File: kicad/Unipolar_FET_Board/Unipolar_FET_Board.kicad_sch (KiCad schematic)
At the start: 18 parts, among them J1 Screw_Terminal_01x04, J3 SENSE, J4 N-MOS, Q1 Q_NMOS_GDS, Q2 Q_NMOS_GDS

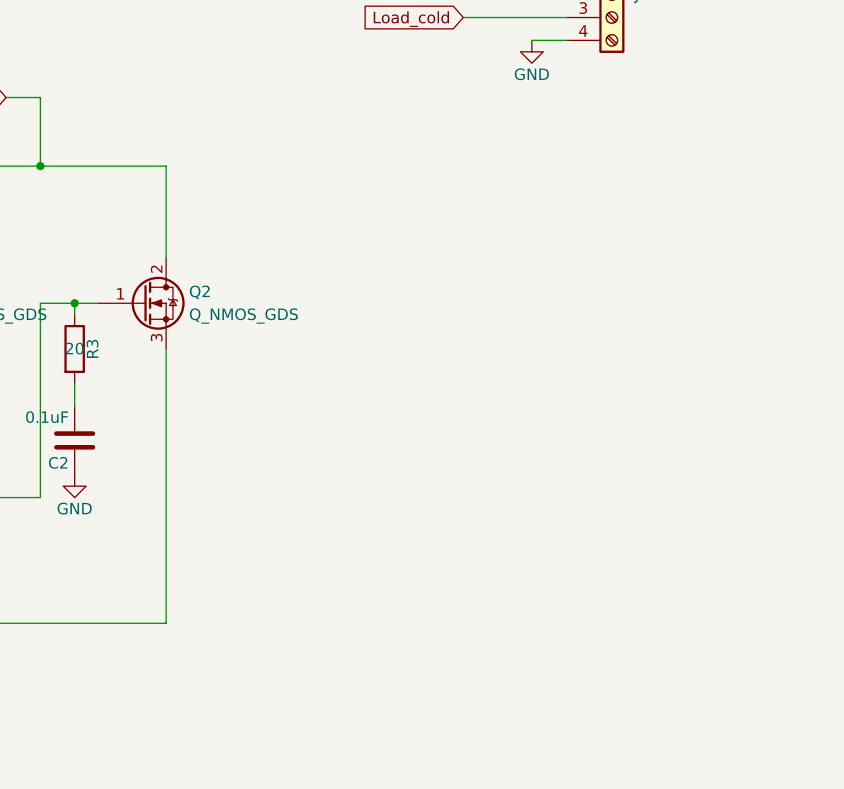
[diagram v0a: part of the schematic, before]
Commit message: Added varistor and labesl for the connecters
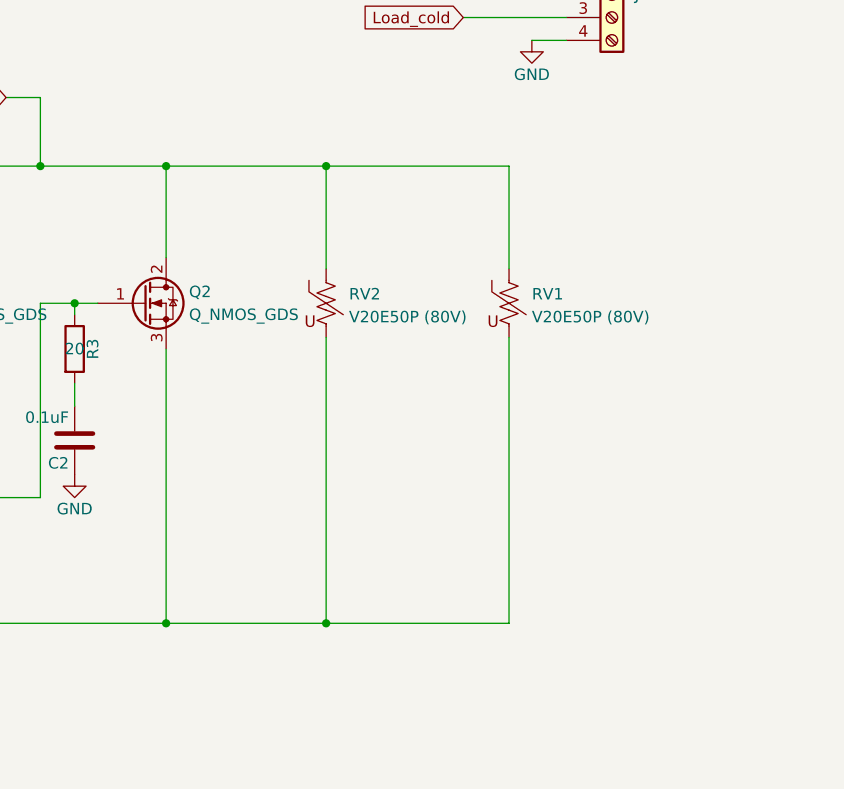
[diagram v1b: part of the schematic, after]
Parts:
- added RV1, RV2: V20E50P (80V), Varistor:RV_Disc_D15.5mm_W7.5mm_P7.5mm, symbol Device:Varistor_US
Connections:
- net Load_cold: now also RV1.1, RV2.1
- net at Q1.3 (S), Q2.3 (S), R9.1: now also RV1.2, RV2.2

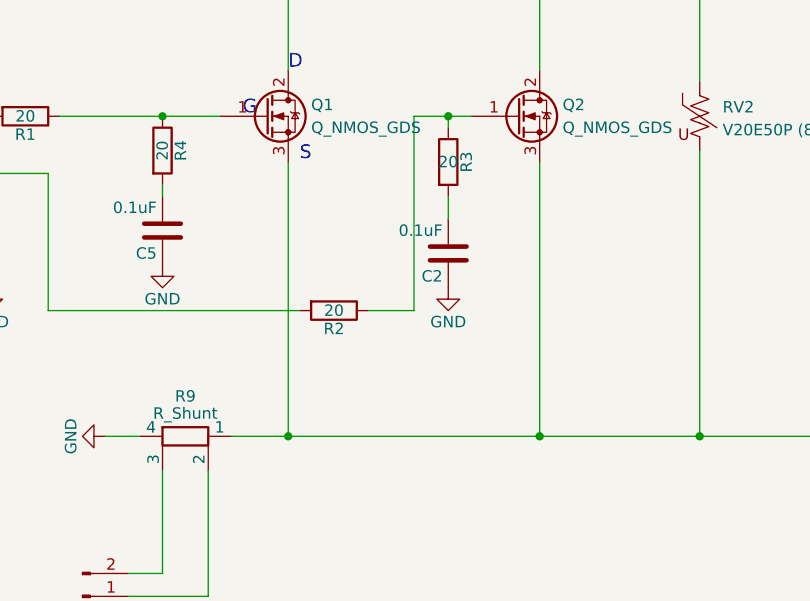
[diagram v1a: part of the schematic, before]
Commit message: Parallel MOS with current sharing resistors
Putting additional resistors in series with the source of each MOS is not necessary.
Nonetheless I saved this partiular snapshot in case we want to pursuit this strategy to share the current
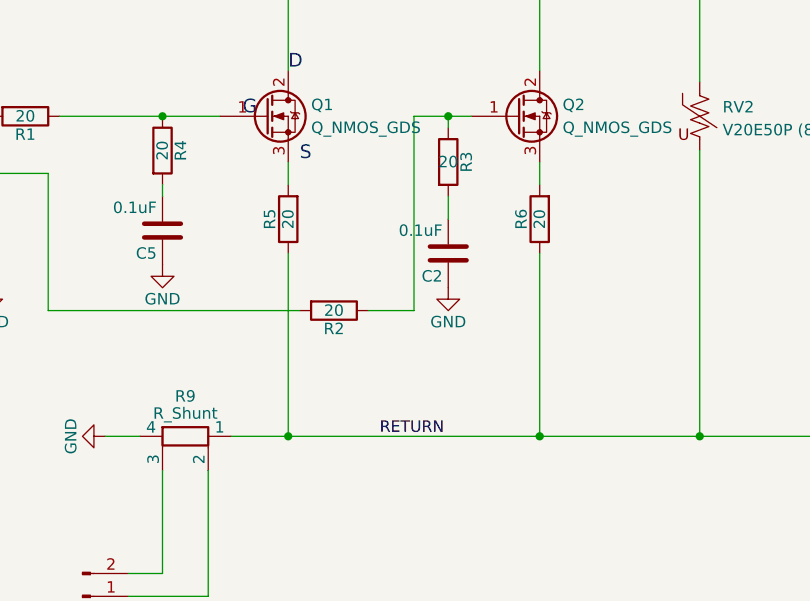
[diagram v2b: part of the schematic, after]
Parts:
- added R5, R6: 20, zmyfootprint:res_2818, symbol rear-rescue:R-rear-rescue
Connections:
- net RETURN: now reaches R9.1, RV1.2, RV2.2
- net RETURN: now also R5.1, R6.1; no longer Q1.3 (S), Q2.3 (S)
- new net: Q1.3 (S), R5.2
- new net: Q2.3 (S), R6.2
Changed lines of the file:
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@@
+	)
+	(junction
+		(at 134.62 104.14)
+		(diameter 0)
+		(color 0 0 0 0)
 	)
 	(junction
@@
 		(color 0 0 0 0)
 	)
-	(junction
-		(at 134.62 104.14)
-		(diameter 0)
-		(color 0 0 0 0)
-	)
 	(wire
 		(pts
@@
 	(wire
 		(pts
+			(xy 162.56 73.66) (xy 162.56 76.2)
+		)
+		(stroke
+			(width 0)
+			(type default)
+		)
+	)
+	(wire
+		(pts
 			(xy 66.04 35.56) (xy 66.04 39.37)
 		)
@@
 	(wire
 		(pts
-			(xy 162.56 73.66) (xy 162.56 104.14)
-		)
-		(stroke
-			(width 0)
-			(type default)
-		)
-	)
-	(wire
-		(pts
 			(xy 109.22 68.58) (xy 120.65 68.58)
 		)
@@
 	(wire
 		(pts
-			(xy 134.62 73.66) (xy 134.62 104.14)
+			(xy 134.62 73.66) (xy 134.62 76.2)
 		)
 		(stroke
@@
 	(wire
 		(pts
+			(xy 162.56 104.14) (xy 134.62 104.14)
+		)
+		(stroke
+			(width 0)
+			(type default)
+		)
+	)
+	(wire
+		(pts
 			(xy 152.4 68.58) (xy 154.94 68.58)
 		)
@@
 	(wire
 		(pts
+			(xy 162.56 83.82) (xy 162.56 104.14)
+		)
+		(stroke
+			(width 0)
+			(type default)
+		)
+	)
+	(wire
+		(pts
 			(xy 200.66 64.77) (xy 200.66 53.34)
 		)
@@
 	(wire
 		(pts
-			(xy 162.56 104.14) (xy 134.62 104.14)
-		)
-		(stroke
-			(width 0)
-			(type default)
-		)
-	)
-	(wire
-		(pts
 			(xy 200.66 31.75) (xy 200.66 33.02)
+		)
+		(stroke
+			(width 0)
+			(type default)
+		)
+	)
+	(wire
+		(pts
+			(xy 134.62 83.82) (xy 134.62 104.14)
 		)
 		(stroke
@@
 			(font
 				(size 1.524 1.524)
+			)
+			(justify left bottom)
+		)
+	)
+	(label "RETURN"
+		(at 144.78 104.14 0)
+		(fields_autoplaced yes)
+		(effects
+			(font
+				(size 1.27 1.27)
 			)
 			(justify left bottom)
@@
 	)
 	(symbol
+		(lib_id "rear-rescue:R-rear-rescue")
+		(at 134.62 80.01 180)
+		(unit 1)
+		(exclude_from_sim no)
+		(in_bom yes)
+		(on_board yes)
+		(dnp no)
+		(property "Reference" "R5"
+			(at 132.588 80.01 90)
+			(effects
+				(font
+					(size 1.27 1.27)
+				)
+			)
+		)
+		(property "Value" "20"
+			(at 134.62 80.01 90)
+			(effects
+				(font
+					(size 1.27 1.27)
+				)
+			)
+		)
+		(property "Footprint" "zmyfootprint:res_2818"
+			(at 136.398 80.01 90)
+			(effects
+				(font
+					(size 1.27 1.27)
+				)
+				(hide yes)
+			)
+		)
+		(property "Datasheet" ""
+			(at 134.62 80.01 0)
+			(effects
+				(font
+					(size 1.27 1.27)
+				)
+				(hide yes)
+			)
+		)
+		(property "Description" ""
+			(at 134.62 80.01 0)
+			(effects
+				(font
+					(size 1.27 1.27)
+				)
+				(hide yes)
+			)
+		)
+		(property "DIGIKEY" "541-3276-1-ND"
+			(at 134.62 80.01 90)
+			(effects
+				(font
+					(size 1.27 1.27)
+				)
+				(hide yes)
+			)
+		)
+		(property "PARTNO" "WSHP2818R0100FEA"
+			(at 134.62 80.01 90)
+			(effects
+				(font
+					(size 1.27 1.27)
+				)
+				(hide yes)
+			)
+		)
+		(pin "1"
+		)
+		(pin "2"
+		)
+		(instances
+			(project "Unipolar_FET_Board"
+				(path "/2f21daab-ac04-42a8-876c-c86138d20a60"
+					(reference "R5")
+					(unit 1)
+				)
+			)
+		)
+	)
+	(symbol
 		(lib_id "Connector:Conn_01x02_Pin")
 		(at 93.98 83.82 0)
@@
 					(unit 1)
 				)
+			)
+		)
+	)
+	(symbol
+		(lib_id "rear-rescue:R-rear-rescue")
+		(at 162.56 80.01 180)
+		(unit 1)
+		(exclude_from_sim no)
+		(in_bom yes)
+		(on_board yes)
+		(dnp no)
+		(property "Reference" "R6"
+			(at 160.528 80.01 90)
+			(effects
+				(font
+					(size 1.27 1.27)
+				)
+			)
+		)
+		(property "Value" "20"
+			(at 162.56 80.01 90)
+			(effects
+				(font
+					(size 1.27 1.27)
+				)
+			)
+		)
+		(property "Footprint" "zmyfootprint:res_2818"
+			(at 164.338 80.01 90)
+			(effects
+				(font
+					(size 1.27 1.27)
+				)
+				(hide yes)
+			)
+		)
+		(property "Datasheet" ""
+			(at 162.56 80.01 0)
+			(effects
+				(font
+					(size 1.27 1.27)
+				)
+				(hide yes)
+			)
+		)
+		(property "Description" ""
+			(at 162.56 80.01 0)
+			(effects
+				(font
+					(size 1.27 1.27)
+				)
+				(hide yes)
+			)
+		)
+		(property "DIGIKEY" "541-3276-1-ND"
+			(at 162.56 80.01 90)
+			(effects
+				(font
+					(size 1.27 1.27)
+				)
+				(hide yes)
+			)
+		)
+		(property "PARTNO" "WSHP2818R0100FEA"
+			(at 162.56 80.01 90)
+			(effects
+				(font
+					(size 1.27 1.27)
+				)
+				(hide yes)
+			)
+		)
+		(pin "1"
+		)
+		(pin "2"
+		)
+		(instances
+			(project "Unipolar_FET_Board"
+				(path "/2f21daab-ac04-42a8-876c-c86138d20a60"
+					(reference "R6")
+					(unit 1)
+				)

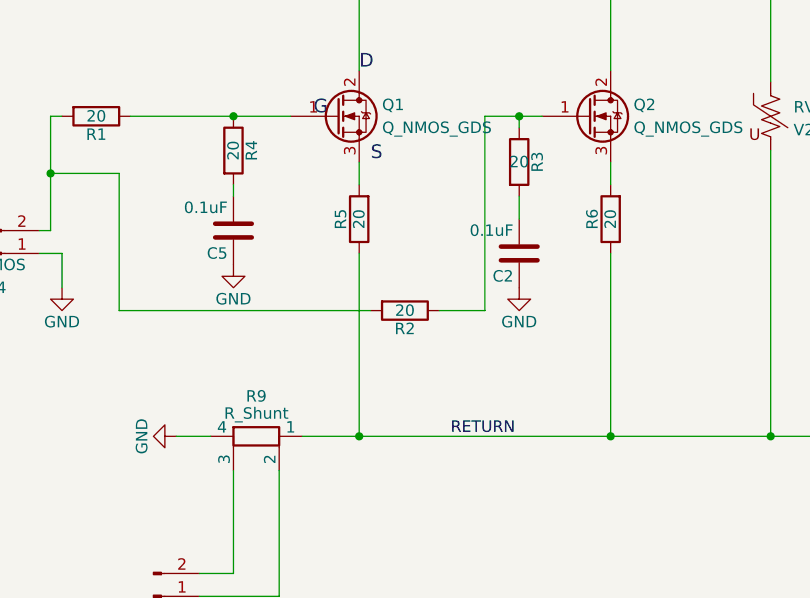
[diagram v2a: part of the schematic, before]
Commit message: The MOS and capacitors are now in the correct orientation
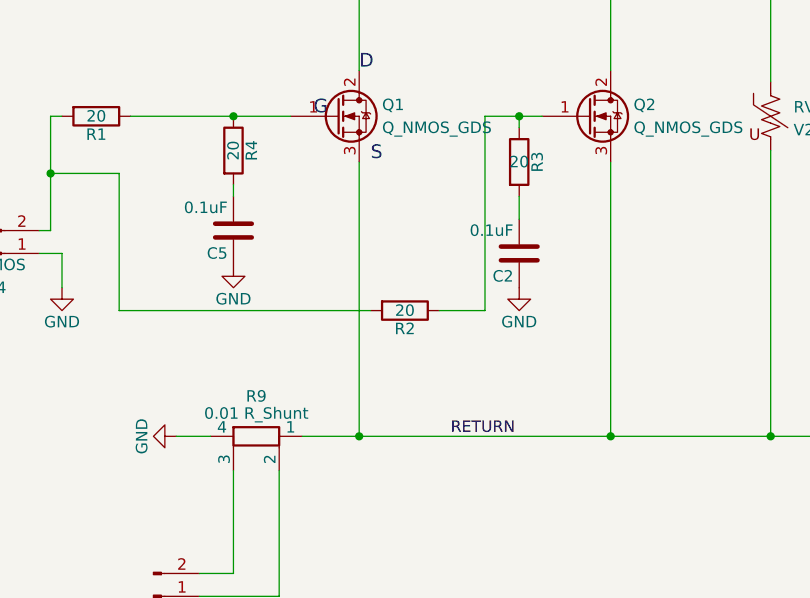
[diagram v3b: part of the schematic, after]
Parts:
- removed R5, R6: 20, zmyfootprint:res_2818, symbol rear-rescue:R-rear-rescue
- C1, C2, C5: DIGIKEY (none) -> 311-1140-1-ND; PARTNO (none) -> CC0805KRX7R9BB104
- C3: footprint CAP_UBY_18X35P5_NCH -> Capacitor_THT:CP_Radial_D18.0mm_P7.50mm; DIGIKEY (none) -> 493-16867-ND; PARTNO (none) -> UKL1J102KHD
- J1: DIGIKEY (none) -> 2453710000-ND; PARTNO (none) -> 2453710000
- Q1, Q2: DIGIKEY (none) -> IXFN520N075T2-ND; DIGIKEY PARTNO IXFN520N075T2-ND -> (none); PARTNO (none) -> IXFN520N075T2
- R9: value R_Shunt -> 0.01 R_Shunt; DIGIKEY (none) -> 696-PCS-0R01D1-ND; PARTNO (none) -> PCS-0R01D1
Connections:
- net RETURN: now also Q1.3 (S), Q2.3 (S)
